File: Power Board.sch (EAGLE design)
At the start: 37 parts, among them Q1 IRLB8743PBF, U1 S18V20F12, U2 D24V22F3, U3 D24V22F5, U4 LTC7004, U5 CD4011BPWR

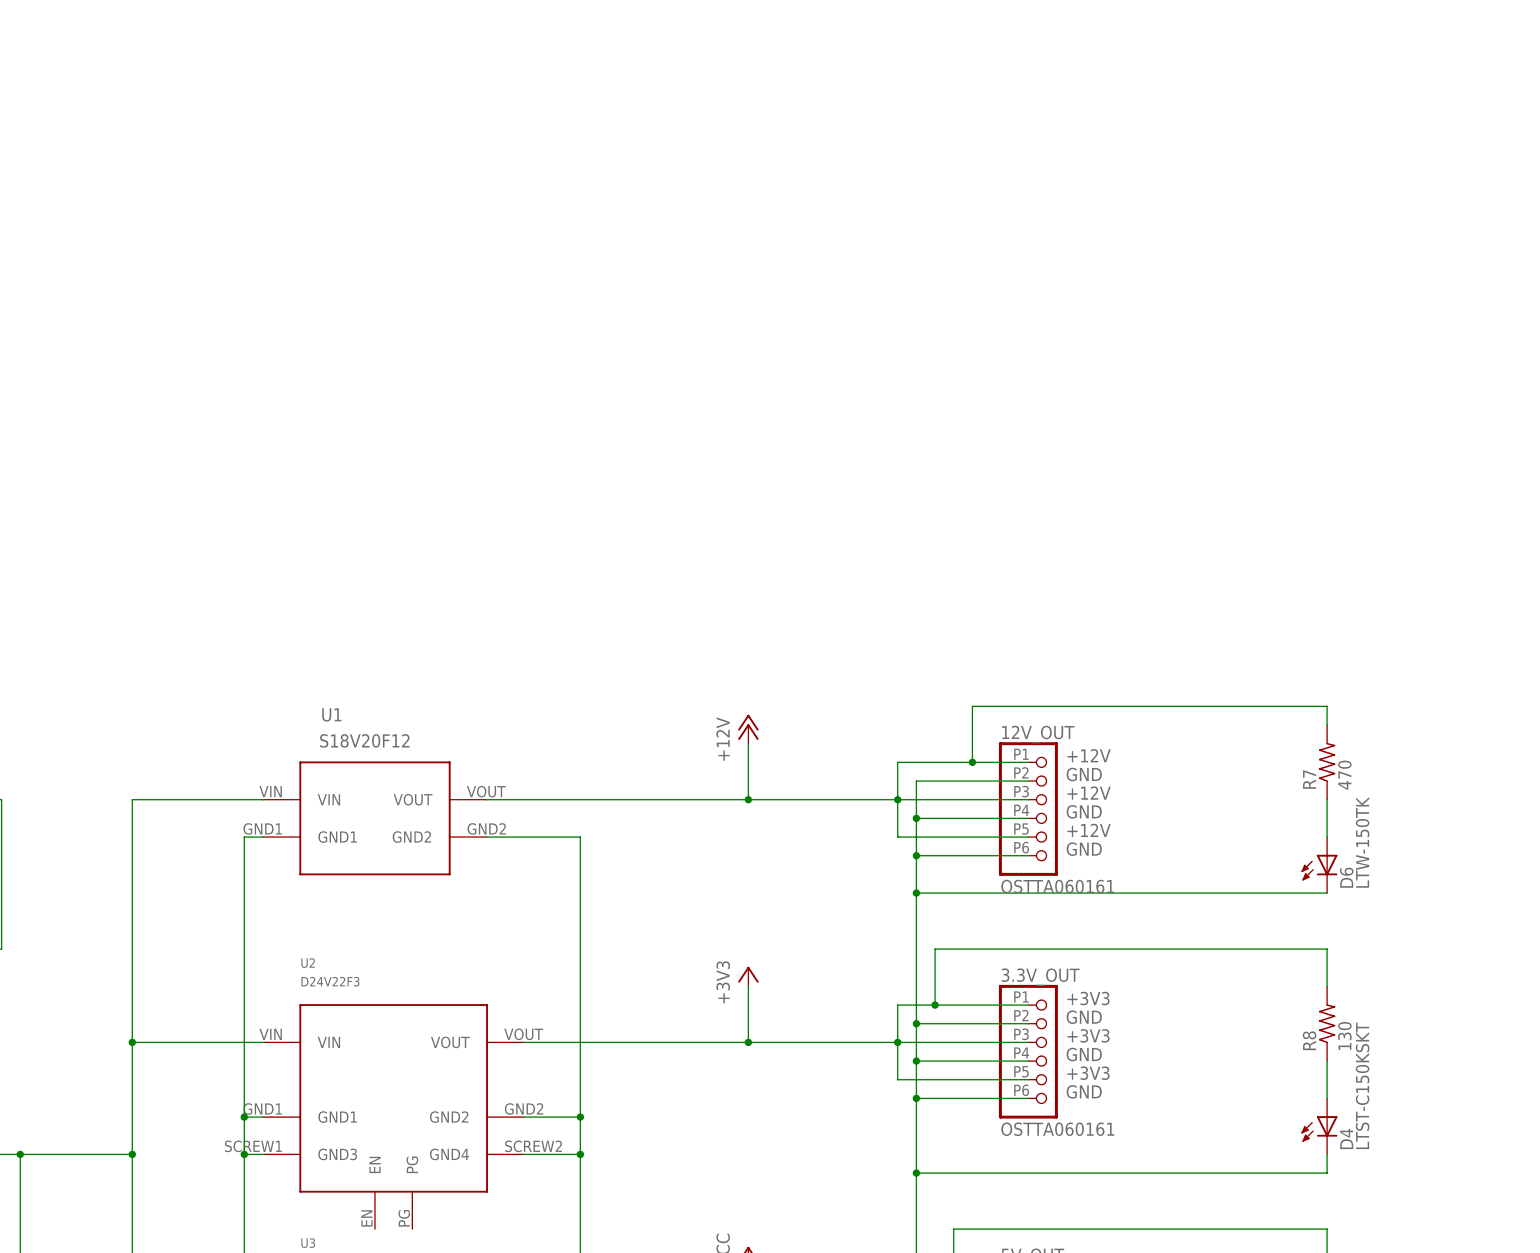
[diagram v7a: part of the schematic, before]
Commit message: Done with Simple Switcher-based voltage regulator
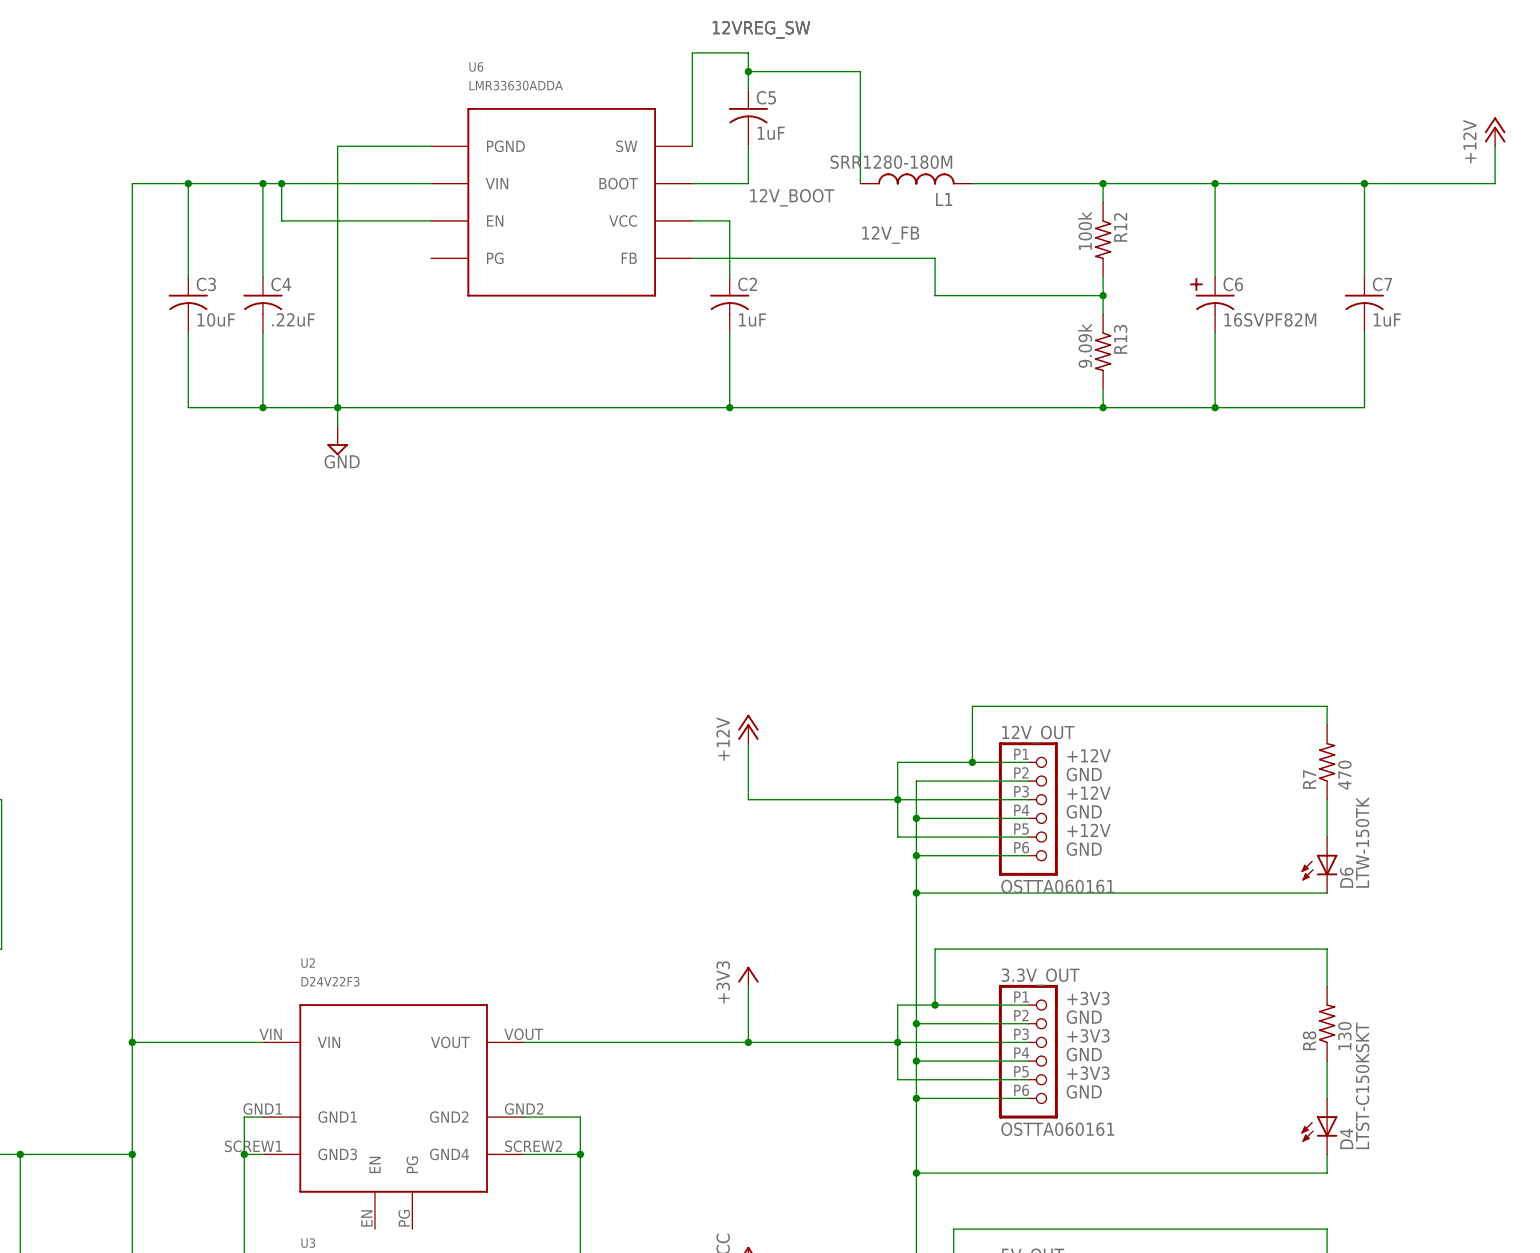
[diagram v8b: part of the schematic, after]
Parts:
- removed U1: S18V20F12, Power Board Custom:S18V20F12
- added C2, C5, C7: 1uF, rcl:C-USC1206
- added C3: 10uF, rcl:C-USC1206
- added C4: .22uF, rcl:C-USC1206
- added C6: 16SVPF82M, Power Board Custom:16SVPF82M
- added L1: SRR1280-180M, Power Board Custom:SRR1280-180M
- added R12: 100k, rcl:R-US_R1206
- added R13: 9.09k, rcl:R-US_R1206
- added U6: LMR33630ADDA, Power Board Custom:LMR33630ADDA
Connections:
- new net 12VREG_SW: C5.1, L1.1, U6.SW
- new net 12V_BOOT: C5.2, U6.BOOT
- new net 12V_FB: R12.2, R13.1, U6.FB
- new net N$8: C2.1, U6.VCC
- net +12V: now also C6.POS, C7.1, L1.2, R12.1; no longer U1.VOUT
- net GND: now also C2.2, C3.2, C4.2, C6.NEG, C7.2, R13.2, U6.PGND; no longer U1.GND1, U1.GND2
- net LOG_VIN: now also C3.1, C4.1, U6.EN, U6.VIN; no longer U1.VIN
